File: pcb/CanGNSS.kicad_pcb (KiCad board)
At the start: 2 copper layers, 66.4 x 28.1 mm, 18 parts, among them IC101 ATTINY3224-SS, P102 CONN_5, P103 CAN, U101 MCP2515, U102 TJA1050, U103 NCP1117ST50T3G, U105 BMP280, X101 8MHz

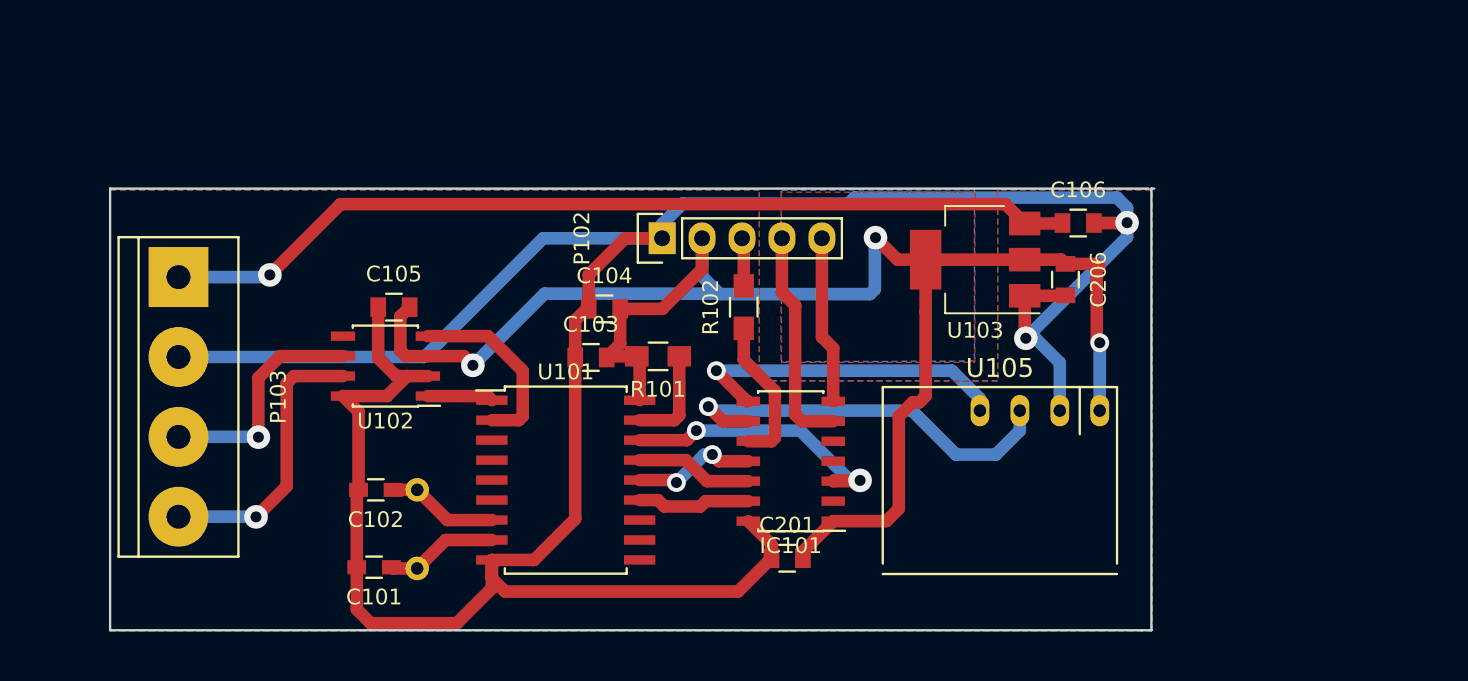
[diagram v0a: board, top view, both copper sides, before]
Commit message: Added ability to configure at startup
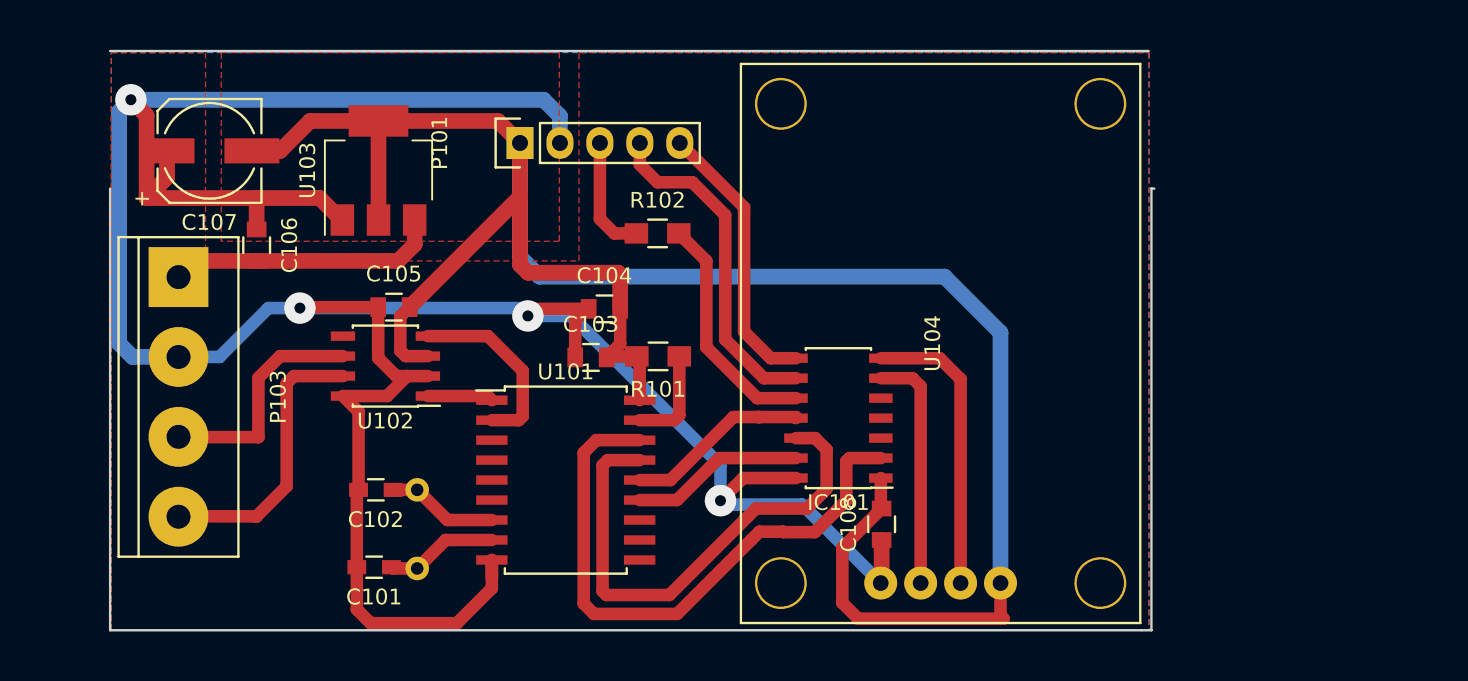
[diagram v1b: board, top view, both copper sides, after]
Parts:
- removed C201: 100nF, Capacitors_SMD:C_0805
- removed C206: 10uF, Capacitors_SMD:C_0805
- removed P102: CONN_5, Pin_Headers:Pin_Header_Straight_1x05
- removed U105: BMP280, Divers:BMP280
- added C107: 100uF, Capacitors_SMD:c_elec_6.3x5.7, F.Cu at (112.3, 106.4)
- added C108: 100nF, Capacitors_SMD:C_0805, F.Cu at (155.0, 130.2)
- added P101: Debug, Pin_Headers:Pin_Header_Straight_1x05, F.Cu at (132.0, 105.9)
- added U104: neo-m8n-module, Divers:neo-m8n-module, F.Cu at (158.8, 118.7)
- R102: value 270R -> 10K
- moved C106 52.3 mm to (115.3, 112.4), turned to 270 degrees
- moved U103 38.4 mm to (123.0, 107.7), turned to 90 degrees
- moved R102 7.21 mm to (140.8, 111.7), turned to 0 degrees
- moved IC101 4.09 mm to (152.3, 123.4)
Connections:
- C106 pad 1: 12v -> GND
- C106 pad 2: GND -> 12v
- IC101 pad 10: UDPI -> Net-(IC101-Pad10)
- IC101 pad 2: (no net) -> CANCS
- IC101 pad 3: CANCS -> (no net)
- IC101 pad 6: RX -> GPSRX
- IC101 pad 7: TX -> GPSTX
- IC101 pad 8: SDA -> DEBUG_TX
- IC101 pad 9: SCL -> DEBUG_RX
- R102 pad 2: Net-(P102-Pad3) -> Net-(IC101-Pad10)
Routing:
- net 12v: track 58.7 -> 17.4 mm, vias 1 -> 0
- net 5V: track 108.3 -> 142.1 mm, vias 3 -> 0
- net SCL: track 25.9 -> 0.00 mm, vias 1 -> 0
- net MISO: track 7.47 -> 32.4 mm
- net DEBUG_RX: track 0.00 -> 21.6 mm
- net SDA: track 21.1 -> 0.00 mm, vias 1 -> 0
- net CANCS: track 19.0 -> 38.3 mm, vias 2 -> 0
- net GPSTX: track 0.00 -> 18.6 mm
- net DEBUG_TX: track 0.00 -> 17.7 mm
- net GPSRX: track 0.00 -> 15.3 mm
- net Net-(IC101-Pad10): track 0.00 -> 15.0 mm
- net RX: track 14.2 -> 0.00 mm
- net TX: track 10.7 -> 0.00 mm
- net GND: track 178.1 -> 188.7 mm, vias 2 -> 4
- net MOSI: track 7.89 -> 11.9 mm, vias 2 -> 0
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- removed copper zone on B.Cu, net 5V
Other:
- board size 66.4 x 28.1 mm -> 66.4 x 36.8 mm
- net class Default: via_dia 1.2 -> 2

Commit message: Updated board and config
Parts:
- removed U104: neo-m8n-module, Divers:neo-m8n-module
- added C1: 10uF, Capacitor_SMD:C_0805_2012Metric_Pad1.18x1.45mm_HandSolder, F.Cu at (144.3, 126.9)
- added D1: D, Diode_SMD:D_0805_2012Metric_Pad1.15x1.40mm_HandSolder, F.Cu at (115.4, 111.0)
- added F1: Polyfuse_Small, Fuse:Fuse_1812_4532Metric_Pad1.30x3.40mm_HandSolder, F.Cu at (115.4, 115.5)
- added JP1: Jumper_2_Bridged, Connector_PinHeader_2.54mm:PinHeader_1x02_P2.54mm_Vertical, F.Cu at (145.9, 104.9)
- added U1: neo-m8n-module-mini, iebSpecials:neo-m8n-module-mini, F.Cu at (170.1, 119.9)
- C101, C102: footprint Resistors_SMD:R_0603_HandSoldering -> Capacitor_SMD:C_0805_2012Metric_Pad1.18x1.45mm_HandSolder
- C103, C104, C105, C106, C108: footprint Capacitors_SMD:C_0805 -> Capacitor_SMD:C_0805_2012Metric_Pad1.18x1.45mm_HandSolder
- C107: value 100uF -> 10uF; footprint Capacitors_SMD:c_elec_6.3x5.7 -> Capacitor_SMD:C_0805_2012Metric_Pad1.18x1.45mm_HandSolder
- IC101: footprint Housings_SOIC:SOIC-14_3.9x8.7mm_Pitch1.27mm -> Package_SO:SO-14_3.9x8.65mm_P1.27mm
- P101: footprint Pin_Headers:Pin_Header_Straight_1x05 -> Connector_PinHeader_2.54mm:PinHeader_1x05_P2.54mm_Vertical
- P103: footprint Connect:bornier4 -> Connector_Wire:SolderWire-1.5sqmm_1x04_P6mm_D1.7mm_OD3mm
- R101: footprint Resistors_SMD:R_0805_HandSoldering -> Resistor_SMD:R_0805_2012Metric_Pad1.20x1.40mm_HandSolder
- R102: value 10K -> 470R; footprint Resistors_SMD:R_0805_HandSoldering -> Resistor_SMD:R_0805_2012Metric_Pad1.20x1.40mm_HandSolder
- U101: footprint Housings_SOIC:SOIC-18W_7.5x11.6mm_Pitch1.27mm -> Package_SO:SOIC-18W_7.5x11.6mm_P1.27mm
- U102: footprint Housings_SOIC:SOIC-8_3.9x4.9mm_Pitch1.27mm -> Package_SO:SO-8_3.9x4.9mm_P1.27mm
- U103: footprint TO_SOT_Packages_SMD:SOT-223-3Lead_TabPin2 -> Package_TO_SOT_SMD:SOT-223-3_TabPin2
- X101: value 8MHz -> 16MHz; footprint Crystals:Resonator-2pin_w10.0mm_h5.0mm -> Crystal:Crystal_SMD_HC49-SD; moved to F.Cu
- moved C101 19.2 mm to (141.9, 133.7), turned to -90 degrees
- moved C107 18.7 mm to (130.0, 112.4), turned to 180 degrees
- moved C103 18.6 mm to (118.0, 121.2)
- moved R101 17.7 mm to (123.2, 117.7), turned to 90 degrees
- moved C104 16.4 mm to (121.1, 117.7), turned to 90 degrees
- moved C108 12.4 mm to (144.2, 124.2), turned to 0 degrees
- moved IC101 12.4 mm to (142.8, 115.4)
- moved U102 9.29 mm to (118.3, 127.8)
- moved C105 9.22 mm to (118.0, 123.4)
- moved P103 8.70 mm to (110.2, 113.4)
- moved X101 8.66 mm to (134.0, 131.1), turned to 180 degrees
- moved R102 7.29 mm to (133.7, 109.9), turned to -90 degrees
- moved U101 7.20 mm to (130.7, 121.5), turned to 90 degrees
- moved C102 6.24 mm to (125.9, 133.4), turned to -90 degrees
- moved P101 3.06 mm to (129.1, 105.1)
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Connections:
- C106 pad 2: 12v -> Net-(D1-K)
- IC101 pad 3: (no net) -> unconnected-(IC101-PA5(AIN5/OUT)-Pad3)
- IC101 pad 4: (no net) -> unconnected-(IC101-PA6(AIN6)-Pad4)
- IC101 pad 5: (no net) -> unconnected-(IC101-PA7(AIN7/EVOUTA)-Pad5)
- U101 pad 10: (no net) -> unconnected-(U101-RX1BF-Pad10)
- U101 pad 11: (no net) -> unconnected-(U101-RX0BF-Pad11)
- U101 pad 12: (no net) -> unconnected-(U101-INT-Pad12)
- U101 pad 3: (no net) -> unconnected-(U101-CLKOUT-Pad3)
- U101 pad 4: (no net) -> unconnected-(U101-TX0RTS-Pad4)
- U101 pad 5: (no net) -> unconnected-(U101-TX1RTS-Pad5)
- U101 pad 6: (no net) -> unconnected-(U101-TX2RTS-Pad6)
- U102 pad 5: (no net) -> unconnected-(U102-Vref-Pad5)
- U103 pad 3: 12v -> Net-(D1-K)
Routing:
- net 5V: track 142.1 -> 112.6 mm
- net GND: track 188.7 -> 164.2 mm, vias 4 -> 1
- net Net-(D1-K): track 0.00 -> 14.8 mm
- net CANCS: track 38.3 -> 23.6 mm
- net CANH: track 18.0 -> 6.72 mm
- net DEBUG_RX: track 21.6 -> 10.4 mm
- net MISO: track 32.4 -> 21.8 mm
- net 5Vswitched: track 0.00 -> 9.41 mm
- net DEBUG_TX: track 17.7 -> 8.42 mm
- net 12v: track 17.4 -> 8.84 mm
- net CANL: track 14.8 -> 6.24 mm
- net Net-(IC101-(UDPI/RESET)_PA0): track 15.0 -> 8.01 mm
- net GPSTX: track 18.6 -> 12.3 mm
- net Net-(U101-OSC2): track 7.08 -> 10.8 mm
- net Net-(U101-OSC1): track 7.17 -> 10.8 mm
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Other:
- board size 66.4 x 36.8 mm -> 89.2 x 38.3 mm
- net class Default removed
